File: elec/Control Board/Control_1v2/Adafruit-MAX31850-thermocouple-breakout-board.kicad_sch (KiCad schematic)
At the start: 48 parts, among them J11 Con_01x02_2.5mm, J2 MAX31850K

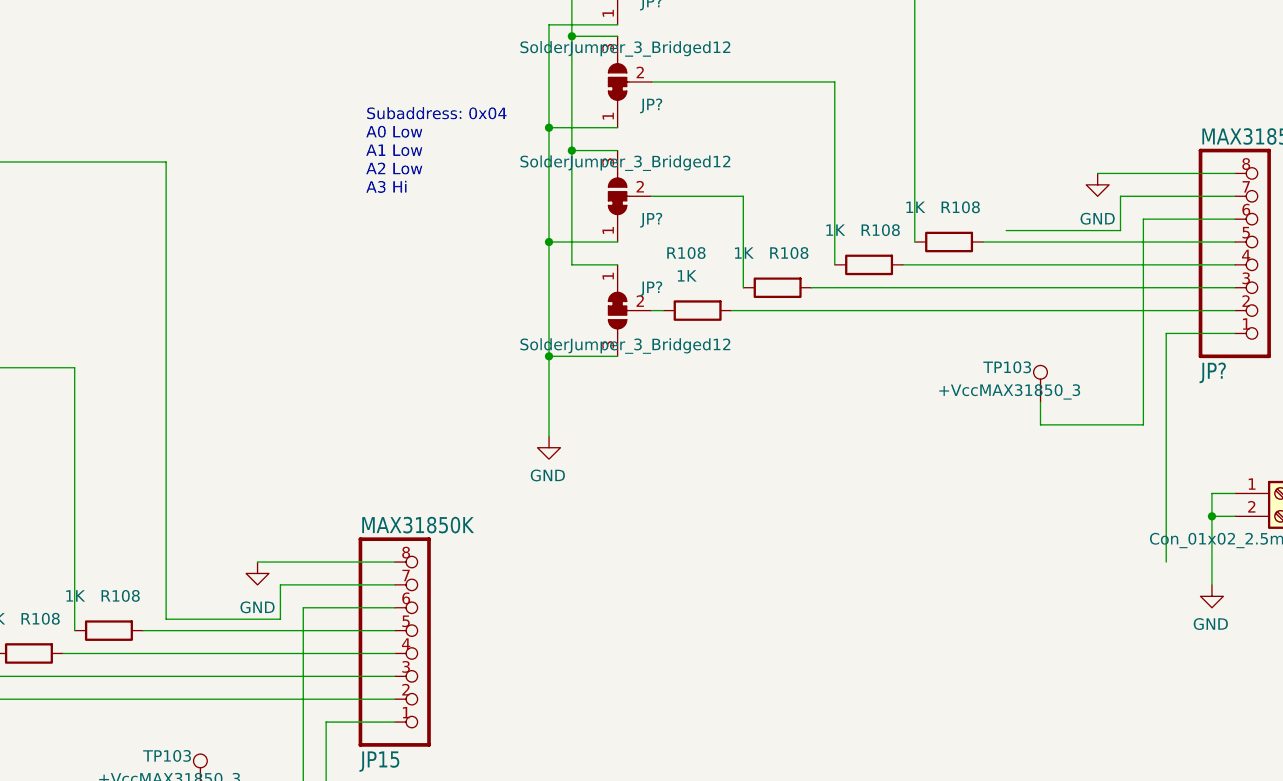
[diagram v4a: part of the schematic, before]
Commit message: Update thermocouple page for power to new amplifier. Update Battery to screw terminal, Update O2 front panel switch and LED connections to JST XH connectors.
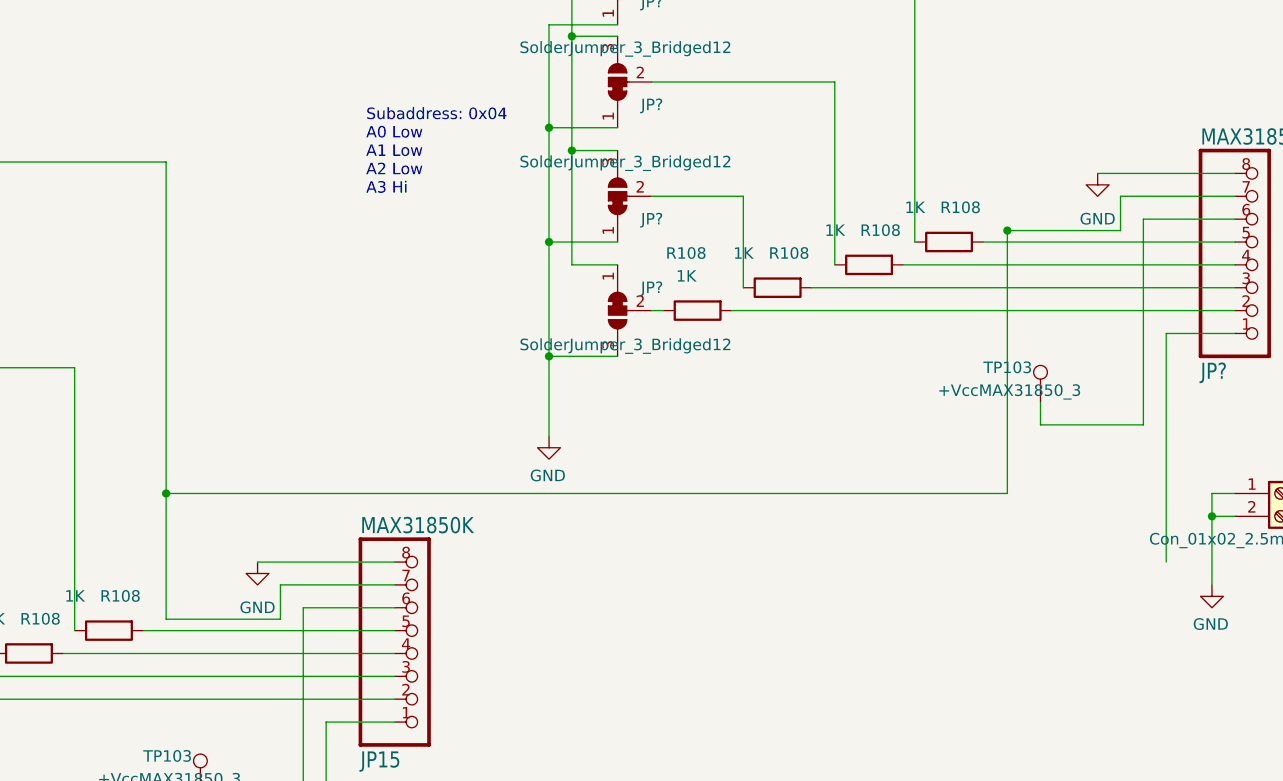
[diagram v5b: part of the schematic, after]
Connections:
- net +VccMAX31850: now also JP?.7
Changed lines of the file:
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@@
     (comment 3 "Drawn By: (Forrest) Lee Erickson")
   )
+  (junction (at 380.492 99.06) (diameter 0) (color 0 0 0 0)
+  )
   (junction (at 238.76 120.65) (diameter 0) (color 0 0 0 0)
   )
@@
   )
   (junction (at 207.01 179.07) (diameter 0) (color 0 0 0 0)
+  )
+  (junction (at 287.02 128.27) (diameter 0) (color 0 0 0 0)
   )
   (junction (at 92.71 121.92) (diameter 0) (color 0 0 0 0)
@@
     (stroke (width 0.1524) (type solid))
   )
+  (wire (pts (xy 380.492 99.06) (xy 393.065 99.06))
+    (stroke (width 0) (type default))
+  )
   (wire (pts (xy 238.76 120.65) (xy 238.76 109.22))
     (stroke (width 0) (type default))
@@
   )
   (wire (pts (xy 121.92 196.85) (xy 114.3 196.85))
+    (stroke (width 0) (type default))
+  )
+  (wire (pts (xy 287.02 128.27) (xy 287.02 142.24))
     (stroke (width 0) (type default))
   )
@@
     (stroke (width 0) (type default))
   )
+  (wire (pts (xy 380.492 99.06) (xy 380.492 128.27))
+    (stroke (width 0) (type default))
+  )
   (wire (pts (xy 332.105 90.17) (xy 332.105 102.87))
     (stroke (width 0) (type default))
@@
     (stroke (width 0) (type default))
   )
-  (wire (pts (xy 287.02 91.44) (xy 287.02 142.24))
+  (wire (pts (xy 287.02 91.44) (xy 287.02 128.27))
     (stroke (width 0) (type default))
   )
@@
     (stroke (width 0) (type default))
   )
-  (wire (pts (xy 380.365 99.06) (xy 393.065 99.06))
+  (wire (pts (xy 380.365 99.06) (xy 380.492 99.06))
     (stroke (width 0) (type default))
   )
@@
     (stroke (width 0) (type default))
   )
+  (wire (pts (xy 380.492 128.27) (xy 287.02 128.27))
+    (stroke (width 0) (type default))
+  )

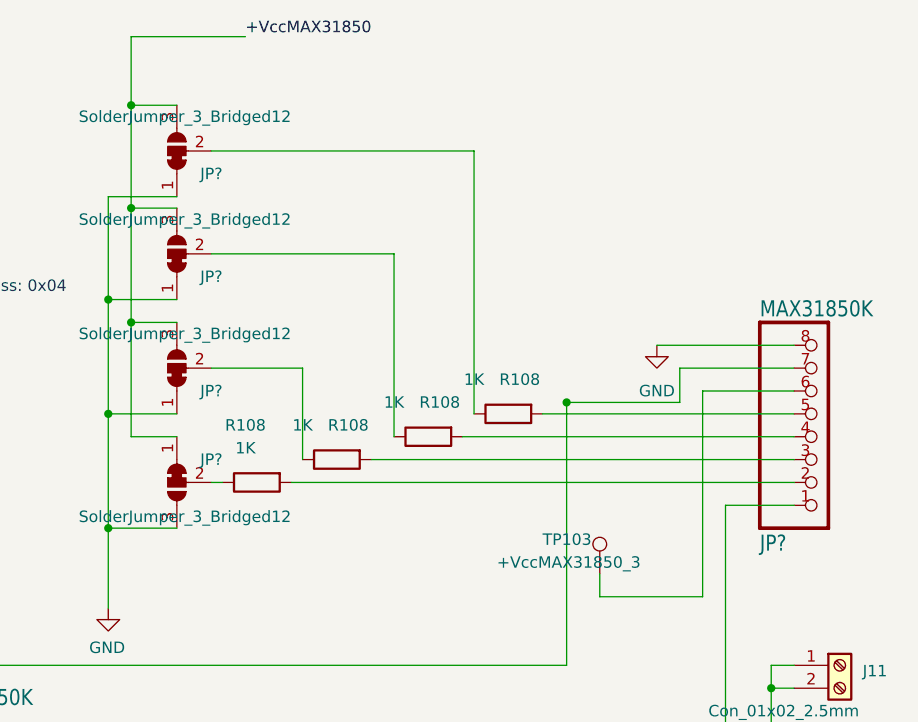
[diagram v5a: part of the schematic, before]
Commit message: Annotation of schematic for new parts in V1.2.
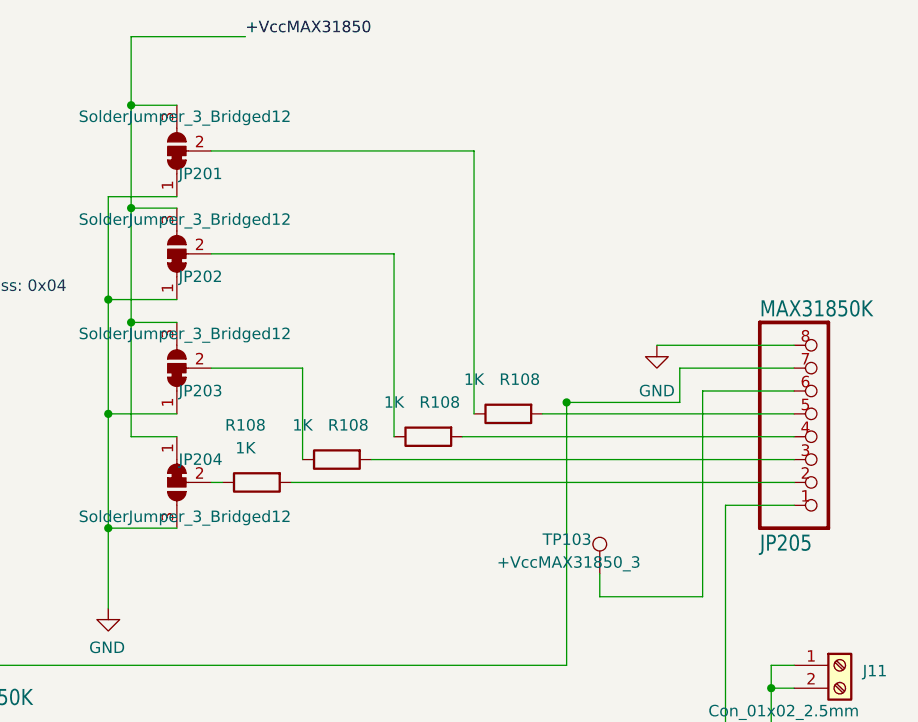
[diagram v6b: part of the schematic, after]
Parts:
- gave numbers to parts that had none: 5
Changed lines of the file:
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@@
         )
         (path "/c68c9deb-8d4d-42f0-adf8-4d3022f4ee59/3ff32a52-b1ed-4756-8661-90a95f721605"
-          (reference "R?") (unit 1)
+          (reference "R202") (unit 1)
         )
       )
@@
   (symbol (lib_id "Control v1-eagle-import:microbuilder_HEADER-1X870MIL") (at 408.305 100.33 0) (mirror x) (unit 1)
     (in_bom yes) (on_board yes) (dnp no)
-    (property "Reference" "JP?" (at 401.955 113.665 0)
+    (property "Reference" "JP205" (at 401.955 113.665 0)
       (effects (font (size 1.778 1.5113)) (justify left bottom))
     )
@@
       (project "Control_1v2"
         (path "/c68c9deb-8d4d-42f0-adf8-4d3022f4ee59/3ff32a52-b1ed-4756-8661-90a95f721605"
-          (reference "JP?") (unit 1)
+          (reference "JP205") (unit 1)
         )
       )
@@
         )
         (path "/c68c9deb-8d4d-42f0-adf8-4d3022f4ee59/3ff32a52-b1ed-4756-8661-90a95f721605"
-          (reference "R?") (unit 1)
+          (reference "R203") (unit 1)
         )
       )
@@
   (symbol (lib_id "Jumper:SolderJumper_3_Bridged12") (at 337.185 107.95 90) (mirror x) (unit 1)
     (in_bom yes) (on_board yes) (dnp no)
-    (property "Reference" "JP?" (at 342.265 105.41 90)
+    (property "Reference" "JP204" (at 342.265 105.41 90)
       (effects (font (size 1.27 1.27)) (justify left))
     )
@@
       (project "Control_1v2"
         (path "/c68c9deb-8d4d-42f0-adf8-4d3022f4ee59/3ff32a52-b1ed-4756-8661-90a95f721605"
-          (reference "JP?") (unit 1)
+          (reference "JP204") (unit 1)
         )
       )
@@
   (symbol (lib_id "Jumper:SolderJumper_3_Bridged12") (at 337.185 95.25 90) (unit 1)
     (in_bom yes) (on_board yes) (dnp no)
-    (property "Reference" "JP?" (at 342.265 97.79 90)
+    (property "Reference" "JP203" (at 342.265 97.79 90)
       (effects (font (size 1.27 1.27)) (justify left))
     )
@@
       (project "Control_1v2"
         (path "/c68c9deb-8d4d-42f0-adf8-4d3022f4ee59/3ff32a52-b1ed-4756-8661-90a95f721605"
-          (reference "JP?") (unit 1)
+          (reference "JP203") (unit 1)
         )
       )
@@
       (project "Control_1v2"
         (path "/c68c9deb-8d4d-42f0-adf8-4d3022f4ee59/3ff32a52-b1ed-4756-8661-90a95f721605"
-          (reference "TP?") (unit 1)
+          (reference "TP201") (unit 1)
         )
       )
@@
         )
         (path "/c68c9deb-8d4d-42f0-adf8-4d3022f4ee59/3ff32a52-b1ed-4756-8661-90a95f721605"
-          (reference "R?") (unit 1)
+          (reference "R201") (unit 1)
         )
       )
@@
         )
         (path "/c68c9deb-8d4d-42f0-adf8-4d3022f4ee59/3ff32a52-b1ed-4756-8661-90a95f721605"
-          (reference "R?") (unit 1)
+          (reference "R204") (unit 1)
         )
       )
@@
   (symbol (lib_id "Jumper:SolderJumper_3_Bridged12") (at 337.185 71.12 90) (unit 1)
     (in_bom yes) (on_board yes) (dnp no)
-    (property "Reference" "JP?" (at 342.265 73.66 90)
+    (property "Reference" "JP201" (at 342.265 73.66 90)
       (effects (font (size 1.27 1.27)) (justify left))
     )
@@
       (project "Control_1v2"
         (path "/c68c9deb-8d4d-42f0-adf8-4d3022f4ee59/3ff32a52-b1ed-4756-8661-90a95f721605"
-          (reference "JP?") (unit 1)
+          (reference "JP201") (unit 1)
         )
       )
@@
         )
         (path "/c68c9deb-8d4d-42f0-adf8-4d3022f4ee59/3ff32a52-b1ed-4756-8661-90a95f721605"
-          (reference "J?") (unit 1)
+          (reference "J201") (unit 1)
         )
       )
@@
   (symbol (lib_id "Jumper:SolderJumper_3_Bridged12") (at 337.185 82.55 90) (unit 1)
     (in_bom yes) (on_board yes) (dnp no)
-    (property "Reference" "JP?" (at 342.265 85.09 90)
+    (property "Reference" "JP202" (at 342.265 85.09 90)
       (effects (font (size 1.27 1.27)) (justify left))
     )
@@
       (project "Control_1v2"
         (path "/c68c9deb-8d4d-42f0-adf8-4d3022f4ee59/3ff32a52-b1ed-4756-8661-90a95f721605"
-          (reference "JP?") (unit 1)
-        )
-      )
+          (reference "JP202") (unit 1)
+        )
+      )

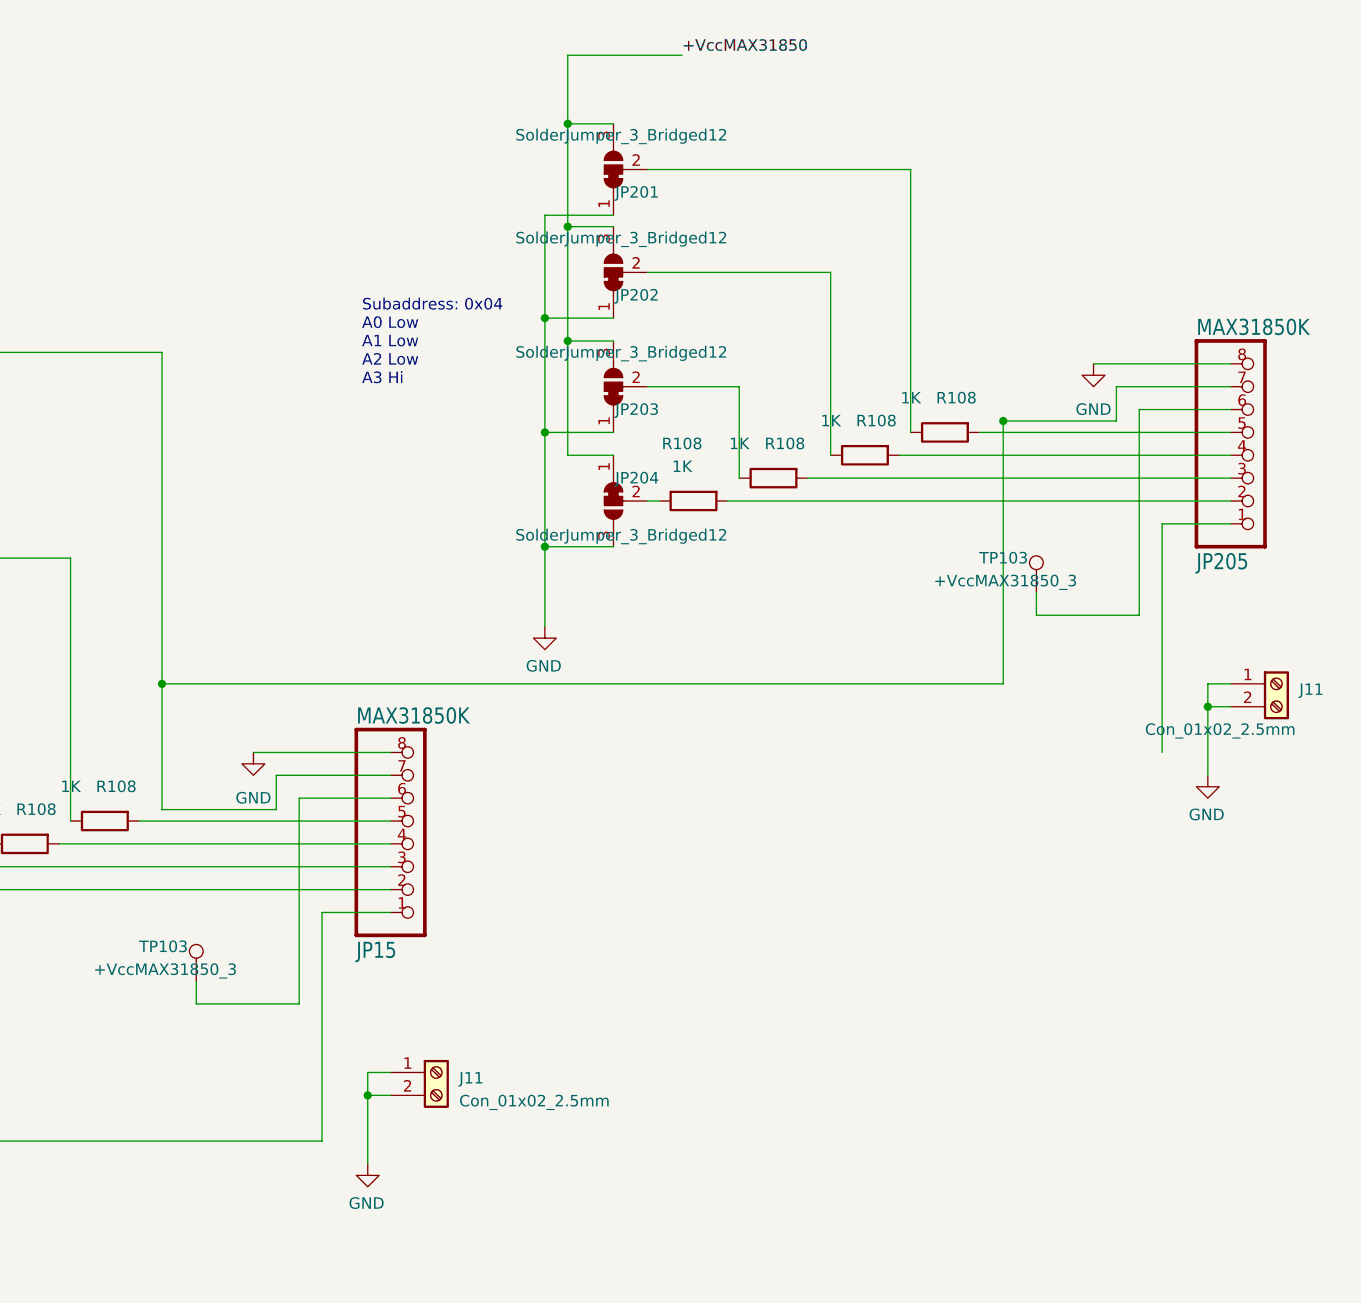
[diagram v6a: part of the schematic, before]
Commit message: Clearing more ERC schematic errors. Off grid. Remove some redundant Net names.
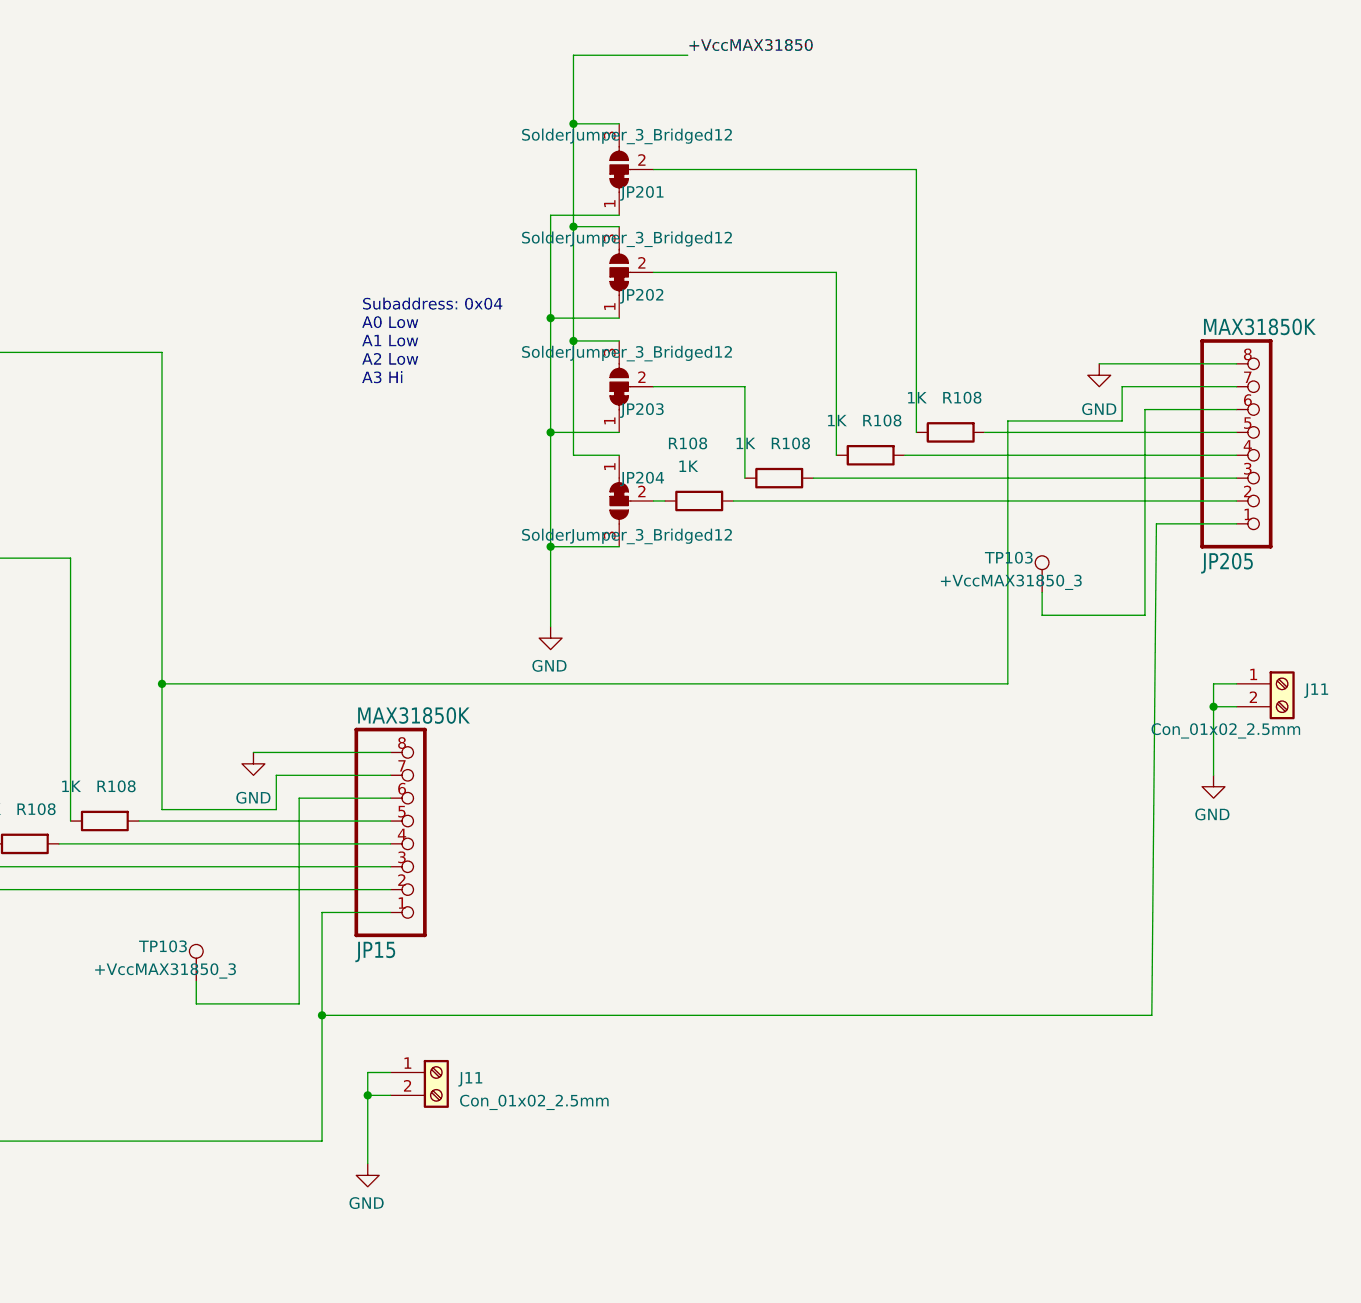
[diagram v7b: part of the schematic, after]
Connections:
- net DATA: now also JP205.1
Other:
- moved on the sheet: J11, JP201, JP202, JP203, JP204, JP205, R108, TP103
